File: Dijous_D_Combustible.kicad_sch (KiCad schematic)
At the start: 33 parts, among them J1 Conn_01x02, J2 DE9_Plug, J3 Conn_01x01, J4 Conn_02x03_Counter_Clockwise, U1 LM2596S-ADJ, U2 LM1117DT-ADJ, U3 MCP2551-I-SN, U4 PIC18F258-I/SO, U5 MCP4725xxx-xCH, Y2 Crystal

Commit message: Add files via upload
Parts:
- C4: value 680uF -> 120uF
- C5: value 3.3nF -> 1nF
- C6: value 220uF -> 470uF
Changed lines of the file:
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@@
 			)
 		)
-		(property "Value" "3.3nF"
+		(property "Value" "1nF"
 			(at 121.92 20.066 90)
 			(effects
@@
 			)
 		)
-		(property "Value" "220uF"
+		(property "Value" "470uF"
 			(at 148.59 55.8799 0)
 			(effects
@@
 			)
 		)
-		(property "Value" "680uF"
+		(property "Value" "120uF"
 			(at 87.63 50.7999 0)
 			(effects

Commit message: Add files via upload
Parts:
- removed J1: Conn_01x02, symbol Connector_Generic:Conn_01x02
- added J5: Screw_Terminal_01x02, symbol Connector:Screw_Terminal_01x02
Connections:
- net GNDPWR: now also J5.1 (Pin_1)
- net Vbat: now also J5.2 (Pin_2)
- net CanH: no longer names the net of C1.1, J2.7, R1.1, U3.7 (CANH)
- net CanL: no longer names the net of C1.2, J2.2, R1.2, U3.6 (CANL)
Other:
- note added: "Conector bateria"
- note added: "Conector botó apertura de combustible o tancament"
- note added: "Cristall"
- note added: "ISCP"
- note added: "Outputs"
- note removed: "Rellotge"
- moved on the sheet: C1, C10, C11, C2, C3, J2, J3, J4, R1, R10, R2, R3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

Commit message: Cambio de nombres
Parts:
- removed J3: Conn_01x01, symbol Connector_Generic:Conn_01x01
- added C12, C13: 100nF, symbol Device:C
- added D2, D3, D4, D5, D8: LED, LED_SMD:LED_0805_2012Metric, symbol Device:LED
- added D6, D7: D, symbol Device:D
- added J1: Conn_01x02, symbol Connector_Generic:Conn_01x02
- added K1, K2: Fujitsu_FTR-LYAA005x, Relay_THT:Relay_SPST-NO_Fujitsu_FTR-LYAA005x_FormA_Vertical, symbol Relay:Fujitsu_FTR-LYAA005x
- added Q1, Q2: 2SC4213, Package_TO_SOT_SMD:SOT-323_SC-70, symbol Transistor_BJT:2SC4213
- added R11, R12: 460, symbol Device:R
- added R13, R15: 510, symbol Device:R
- added R14, R16: 1k, symbol Device:R
- added R17: 515, symbol Device:R
- added R18: 0, symbol Device:R
- added R19, R20: 10K, symbol Device:R
- C3: value 10nF -> 100nF
- R10, R9: value 10K -> R
- Y2: value Crystal -> HC-49-US
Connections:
- net Boto: now also J1.2 (Pin_2)
- net GND: now also C3.2, R10.2, R9.2, C12.2, C13.1, R17.2, R18.2; no longer U1.3 (GND), U1.5 (~{ON}/OFF)
- net GNDPWR: now also U1.3 (GND), U1.5 (~{ON}/OFF), D2.1 (K), D3.1 (K), J1.1 (Pin_1), K1.13, K2.13, Q1.2 (E), Q2.2 (E), R18.1
- net LED_pneumatics: now also D8.2 (A)
- net SCA: now also R19.2; no longer R9.2
- net SCL: now also R20.2; no longer R10.2
- net VCC: now also C3.1, C12.1, C13.2, R19.1, R20.1; no longer R10.1, R9.1
- net Vbat: now also D6.1 (K), D7.1 (K), K1.A1, K2.A1, R11.1, R12.1, R13.1, R15.1
- new net: Q2.1 (B), R16.2
- new net: D4.1 (K), D6.2 (A), K1.A2, Q1.3 (C)
- new net: D5.1 (K), D7.2 (A), K2.A2, Q2.3 (C)
- new net: Q1.1 (B), R14.2
- new net: D8.1 (K), R17.1
- new net: D4.2 (A), R13.2
- new net: D3.2 (A), R12.2
- new net: D2.2 (A), R11.2
- new net: D5.2 (A), R15.2
- new net Bomba de combustible: K2.14
- new net R_Bomba: R10.1, R16.1
- new net R_Dipòsit: R14.1, R9.1
- new net Solenoide: K1.14
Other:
- note added: "LED POWER"
- note added: "LED POWER = Vermell"
- note added: "Outputs i Reles"
- note added: "RELAY STATUS LED"
- note added: "RELAY STATUS LED = Blau"
- note added: "Relè Bomba de Combustible"
- note added: "Relè Tancament Diposit"
- note added: "Sortida Pressió Pneumàtics"
- note added: "Unificació de GNDs"
- note added: "Vcc = 5V"
- note removed: "Outputs"
- moved on the sheet: C3

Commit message: Ultim canvi esquemàtic
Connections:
- net LED_pneumatics: now also U4.3 (RA1/AN1)
- net R_Bomba: now also U4.13 (RC2/CCP1)
- no-connect marks 11 -> 16
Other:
- moved on the sheet: D8, R17, R18, R19, R20

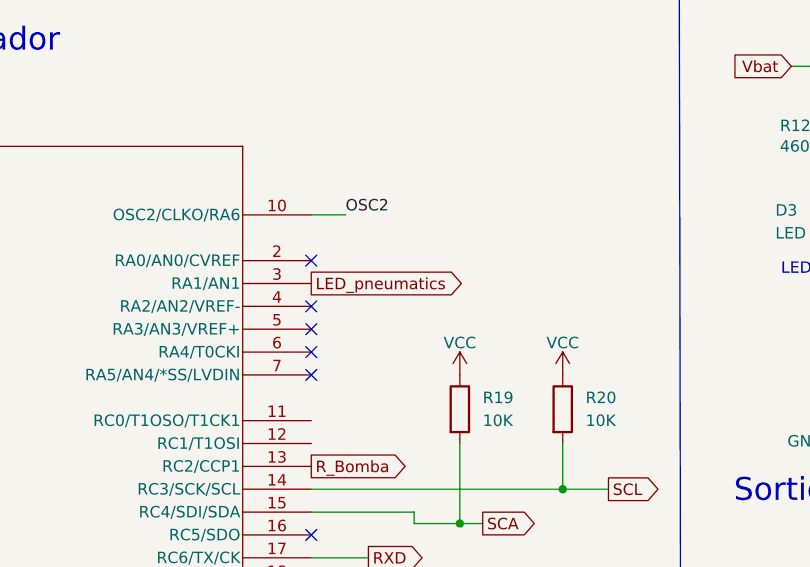
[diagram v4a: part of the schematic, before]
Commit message: Diagrama de blocs actualitzat i esquema
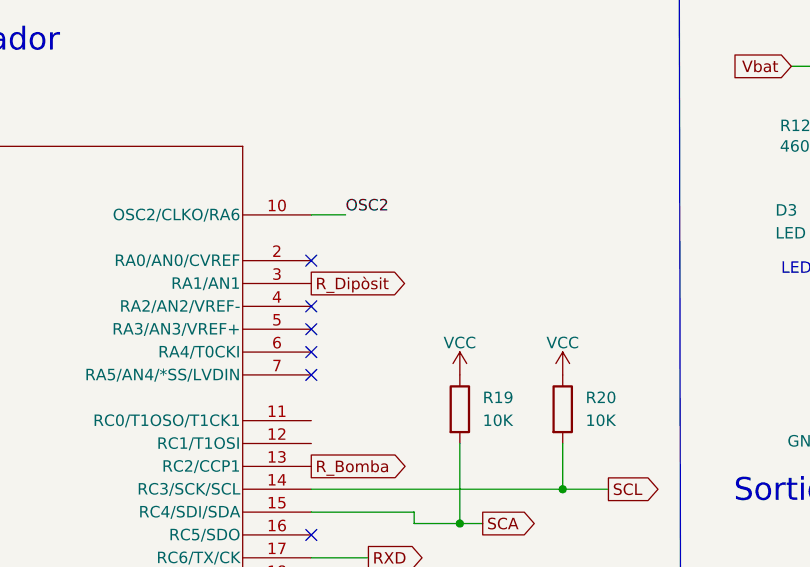
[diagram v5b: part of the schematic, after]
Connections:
- net LED_pneumatics: no longer U4.3 (RA1/AN1)
- net R_Dipòsit: now also U4.3 (RA1/AN1)
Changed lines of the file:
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@@
-		)
-	)
-	(global_label "LED_pneumatics"
-		(shape output)
-		(at 262.89 111.76 0)
-		(fields_autoplaced yes)
-		(effects
-			(font
-				(size 1.27 1.27)
-			)
-			(justify left)
-		)
-		(property "Intersheetrefs" "${INTERSHEET_REFS}"
-			(at 281.115 111.76 0)
-			(effects
-				(font
-					(size 1.27 1.27)
-				)
-				(justify left)
-				(hide yes)
-			)
 		)
 	)
@@
 				(hide yes)
 			)
+		)
+	)
+	(global_label "R_Dipòsit"
+		(shape output)
+		(at 262.89 111.76 0)
+		(fields_autoplaced yes)
+		(effects
+			(font
+				(size 1.27 1.27)
+			)
+			(justify left)
+		)
+		(property "Intersheetrefs" "${INTERSHEET_REFS}"
+			(at 274.6442 111.76 0)
+			(effects
+				(font
+					(size 1.27 1.27)
+				)
+				(justify left)
+				(hide yes)
+			)

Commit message: Readme & Esquemàtic
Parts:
- removed C2: 10nF, symbol Device:C
- removed C8: 11u, symbol Device:C
- removed D3: LED, LED_SMD:LED_0805_2012Metric, symbol Device:LED
- removed D6, D7: D, symbol Device:D
- removed J5: Screw_Terminal_01x02, symbol Connector:Screw_Terminal_01x02
- removed R7: 220, symbol Device:R
- removed R8: 680, symbol Device:R
- removed U2: LM1117DT-ADJ, Package_TO_SOT_SMD:TO-252-3_TabPin2, symbol Regulator_Linear:LM1117DT-ADJ
- added D10: MBR340, Diode_THT:D_DO-201AD_P15.24mm_Horizontal, symbol Diode:MBR340
- added D3, D6, D7, D9: 1N5408, Diode_THT:D_DO-201AD_P15.24mm_Horizontal, symbol Diode:1N5408
- added J3: Screw_Terminal_01x02, TerminalBlock:TerminalBlock_Altech_AK300-2_P5.00mm, symbol Connector:Screw_Terminal_01x02
- added U6: LM1117DT-5.0, Package_TO_SOT_SMD:TO-252-3_TabPin2, symbol Regulator_Linear:LM1117DT-5.0
- C1, C12, C13, C3: footprint (none) -> Capacitor_SMD:C_1206_3216Metric
- C5: footprint (none) -> Capacitor_SMD:C_0603_1608Metric
- C7: footprint (none) -> Capacitor_Tantalum_SMD:CP_EIA-3528-12_Kemet-T
- C9: footprint (none) -> Capacitor_Tantalum_SMD:CP_EIA-3216-12_Kemet-S
- J1: footprint (none) -> Connector_PinHeader_2.00mm:PinHeader_2x01_P2.00mm_Vertical
- J2: footprint (none) -> Connector_Dsub:DSUB-9_Male_Vertical_P2.77x2.84mm
- J4: footprint (none) -> Connector_PinHeader_2.54mm:PinHeader_2x03_P2.54mm_Vertical
- L1: footprint (none) -> Inductor_SMD:L_1206_3216Metric
- R1, R11, R13, R14, R15, R16, R17, R18, R19, R20, R4, R5, R6: footprint (none) -> Resistor_SMD:R_1206_3216Metric
- R10: value R -> 4,7k; footprint (none) -> Resistor_SMD:R_1206_3216Metric
- R12: value 460 -> 60; footprint (none) -> Resistor_SMD:R_1206_3216Metric
- R2, R3: value 10k -> 4,7k; footprint (none) -> Resistor_SMD:R_1206_3216Metric
- R9: value R -> 4.9K; footprint (none) -> Resistor_SMD:R_1206_3216Metric
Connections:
- net Bomba de combustible: now also D3.1 (K), D3.2 (A)
- net Boto: now also R2.1
- net GND: now also C1.2, J1.1 (Pin_1), R3.2, U6.1 (GND); no longer J2.3
- net GNDPWR: now also J3.1 (Pin_1); no longer J1.1 (Pin_1)
- net MCLR: now also R3.1
- net R_Bomba: no longer U4.13 (RC2/CCP1)
- net R_Dipòsit: no longer U4.3 (RA1/AN1)
- net Solenoide: now also D9.1 (K), D9.2 (A)
- net VCC: no longer C12.1, C13.2, C3.1, J4.2 (Pin_2), R3.1, U3.3 (VDD), U4.20 (VDD), U5.3 (VDD)
- net Vbat: now also D10.2 (A), D6.1 (K), D7.1 (K), J3.2 (Pin_2); no longer C4.1, R12.1, R5.2, U1.1 (VIN)
- net at D4.1 (K), K1.A2, Q1.3 (C): now also D6.2 (A)
- net at D5.1 (K), K2.A2, Q2.3 (C): now also D7.2 (A)
- net at J2.7, U3.7 (CANH): now also R12.1; no longer C1.1, R1.1
- net at J2.2, R1.2, U3.6 (CANL): no longer C1.2
- net at R12.2: now also C1.1, R1.1
- net at C5.2, C6.1, C7.1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: now also U6.3 (VI)
- net Vcc: no longer names the net of J2.9
- net Vcc: no longer C9.1
- new net: C4.1, D10.1 (K), R5.2, U1.1 (VIN)
- new net +5V: C12.1, C13.2, C3.1, C9.1, J4.2 (Pin_2), U3.3 (VDD), U4.20 (VDD), U5.3 (VDD), U6.2 (VO)
- now unconnected: U3.5 (Vref)
- no-connect marks 16 -> 23
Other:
- note added: "Freqüència del cristall = 8mhz"
- note removed: "Condensador datasheet"
- note removed: "Condensador:"
- moved on the sheet: C1, D5, D8, K2, Q2, R10, R15, R16, R17, R19, R20

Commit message: README & Layout
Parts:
- removed C12, C13: 100nF, Capacitor_SMD:C_1206_3216Metric, symbol Device:C
- removed D1: 1N5822, Diode_THT:D_DO-201AD_P15.24mm_Horizontal, symbol Diode:1N5822
- removed D10: MBR340, Diode_THT:D_DO-201AD_P15.24mm_Horizontal, symbol Diode:MBR340
- removed D2, D4, D5, D8: LED, LED_SMD:LED_0805_2012Metric, symbol Device:LED
- removed D3, D6, D7: 1N5408, Diode_THT:D_DO-201AD_P15.24mm_Horizontal, symbol Diode:1N5408
- removed J1: Conn_01x02, Connector_PinHeader_2.00mm:PinHeader_2x01_P2.00mm_Vertical, symbol Connector_Generic:Conn_01x02
- removed J2: DE9_Plug, Connector_Dsub:DSUB-9_Male_Vertical_P2.77x2.84mm, symbol Connector:DE9_Plug
- removed J3: Screw_Terminal_01x02, TerminalBlock:TerminalBlock_Altech_AK300-2_P5.00mm, symbol Connector:Screw_Terminal_01x02
- removed J4: Conn_02x03_Counter_Clockwise, Connector_PinHeader_2.54mm:PinHeader_2x03_P2.54mm_Vertical, symbol Connector_Generic:Conn_02x03_Counter_Clockwise
- removed R20: 10K, Resistor_SMD:R_1206_3216Metric, symbol Device:R
- removed U1: LM2596S-ADJ, Package_TO_SOT_SMD:TO-263-5_TabPin3, symbol Regulator_Switching:LM2596S-ADJ
- removed U3: MCP2551-I-SN, Package_SO:SOIC-8_3.9x4.9mm_P1.27mm, symbol Interface_CAN_LIN:MCP2551-I-SN
- removed U4: PIC18F258-I/SO, Librery_SOIC28:SOIC28-W_MC_MCH, symbol PIC18F258-I/SO:PIC18F258-I_SO
- removed U6: LM1117DT-5.0, Package_TO_SOT_SMD:TO-252-3_TabPin2, symbol Regulator_Linear:LM1117DT-5.0
- removed Y2: HC-49-US, Crystal:Crystal_SMD_HC49-SD, symbol Device:Crystal
- added C2: 120uF, Capacitor_SMD:CP_Elec_10x10, symbol Device:C
- added C8: 10u, Capacitor_Tantalum_SMD:CP_EIA-3528-12_Kemet-T, symbol Device:C
- added D1: MBR340, Diode_THT:D_DO-201AD_P15.24mm_Horizontal, symbol Diode:MBR340
- added D10, D3, D6, D7: LED, LED_SMD:LED_0805_2012Metric, symbol Device:LED
- added D2: 1N5822, Diode_THT:D_DO-201AD_P15.24mm_Horizontal, symbol Diode:1N5822
- added D4, D5, D8: 1N5408, Diode_THT:D_DO-201AD_P15.24mm_Horizontal, symbol Diode:1N5408
- added J1: Screw_Terminal_01x02, TerminalBlock:TerminalBlock_Altech_AK300-2_P5.00mm, symbol Connector:Screw_Terminal_01x02
- added J2: Conn_01x02, Connector_PinHeader_2.00mm:PinHeader_2x01_P2.00mm_Vertical, symbol Connector_Generic:Conn_01x02
- added J3: Conn_02x03_Counter_Clockwise, Connector_PinHeader_2.54mm:PinHeader_2x03_P2.54mm_Vertical, symbol Connector_Generic:Conn_02x03_Counter_Clockwise
- added J4: DE9_Plug, Connector_Dsub:DSUB-9_Male_Vertical_P2.77x2.84mm, symbol Connector:DE9_Plug
- added J5, J6, J7: Conn_01x02, Connector_PinHeader_2.54mm:PinHeader_1x02_P2.54mm_Vertical, symbol Connector_Generic:Conn_01x02
- added JP1: Jumper_3_Open, Connector:FanPinHeader_1x03_P2.54mm_Vertical, symbol Jumper:Jumper_3_Open
- added R7, R8: 4,7k, Resistor_SMD:R_1206_3216Metric, symbol Device:R
- added SW1: SW_Push, Button_Switch_SMD:SW_Push_SPST_NO_Alps_SKRK, symbol Switch:SW_Push
- added U1: MCP2551-I-SN, Package_SO:SOIC-8_3.9x4.9mm_P1.27mm, symbol Interface_CAN_LIN:MCP2551-I-SN
- added U2: LM2596S-ADJ, Package_TO_SOT_SMD:TO-263-5_TabPin3, symbol Regulator_Switching:LM2596S-ADJ
- added U3: PIC18F258-I/SO, Librery_SOIC28:SOIC28-W_MC_MCH, symbol PIC18F258-I/SO:PIC18F258-I_SO
- added U4: LM1117DT-5.0, Package_TO_SOT_SMD:TO-252-3_TabPin2, symbol Regulator_Linear:LM1117DT-5.0
- added Y1: HC-49-US, Crystal:Crystal_SMD_HC49-SD, symbol Device:Crystal
- C1: value 100pF -> 100nF
- C10: value 15p -> 22u; footprint Capacitor_SMD:C_0805_2012Metric -> Capacitor_Tantalum_SMD:CP_EIA-3216-12_Kemet-S
- C11: value 15p -> 100nF; footprint Capacitor_SMD:C_0805_2012Metric -> Capacitor_SMD:C_1206_3216Metric
- C3: value 100nF -> 15p; footprint Capacitor_SMD:C_1206_3216Metric -> Capacitor_SMD:C_0805_2012Metric
- C4: value 120uF -> 100pF; footprint Capacitor_THT:CP_Radial_D10.0mm_P5.00mm -> Capacitor_SMD:C_1206_3216Metric
- C5: value 1nF -> 15p; footprint Capacitor_SMD:C_0603_1608Metric -> Capacitor_SMD:C_0805_2012Metric
- C6: value 470uF -> 1nF; footprint Capacitor_SMD:CP_Elec_10x10 -> Capacitor_SMD:C_0603_1608Metric
- C7: value 10u -> 470uF; footprint Capacitor_Tantalum_SMD:CP_EIA-3528-12_Kemet-T -> Capacitor_SMD:CP_Elec_10x10
- C9: value 22u -> 100nF; footprint Capacitor_Tantalum_SMD:CP_EIA-3216-12_Kemet-S -> Capacitor_SMD:C_1206_3216Metric
- R1: value 60 -> 15k
- R10: value 4,7k -> 510
- R11: value 460 -> 4,7k
- R12: value 60 -> 1k
- R13: value 510 -> 10K
- R14: value 1k -> 10K
- R15: value 510 -> 460
- R16: value 1k -> 510
- R17: value 515 -> 4.7K
- R18: value 0 -> 1k
- R19: value 10K -> 515
- R2, R3: value 4,7k -> 60
- R4: value 15k -> 0
- R9: value 4.9K -> 10k; footprint Resistor_SMD:R_1206_3216Metric -> Resistor_SMD:R_0805_2012Metric
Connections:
- net Bomba de combustible is gone; now on net Vbat: K2.14
- net +5V: now also C1.1, C10.1, C11.1, C9.2, R13.1, R14.1, R9.1, J3.2 (Pin_2), U1.3 (VDD), U3.20 (VDD), U4.2 (VO); no longer C3.1, C9.1
- net Boto: now also J2.2 (Pin_2), R8.1, U3.21 (RB0/INT0); no longer R2.1
- net GND: now also C11.2, C5.1, C9.1, R1.2, R11.2, R19.2, C8.2, J2.1 (Pin_1), J3.3 (Pin_3), J6.2 (Pin_2), R7.2, R8.2, SW1.2, U1.2 (VSS), U3.19 (VSS), U3.8 (VSS), U4.1 (GND); no longer C11.1, C6.2, C7.2, C9.2, R10.2, R18.2, R2.2, R3.2, R9.2
- net GNDPWR: now also C7.2, D9.2 (A), R4.1, C2.2, D2.2 (A), D5.2 (A), D6.1 (K), J1.1 (Pin_1), J5.2 (Pin_2), J7.2 (Pin_2), U2.3 (GND), U2.5 (~{ON}/OFF); no longer K1.13, K2.13, R18.1
- net LED_pneumatics: now also D10.2 (A), U3.22 (RB1/INT1)
- net MCLR: now also J3.1 (Pin_1), JP1.1 (A), R7.1; no longer R3.1
- net Nivell_combustible: now also J6.1 (Pin_1)
- net OSC1: now also C3.1, U3.9 (OSC1/CLKI), Y1.1; no longer C10.1
- net OSC2: now also C5.2, U3.10 (OSC2/CLKO/RA6), Y1.2; no longer C11.2
- net PGC: now also J3.5 (Pin_5), U3.27 (RB6/PGC)
- net PGD: now also J3.4 (Pin_4), U3.28 (RB7/PGD)
- net RXD: now also U1.4 (RXD), U3.17 (RC6/TX/CK)
- net R_Bomba: now also R11.1, R12.1, U3.13 (RC2/CCP1); no longer R10.1, R16.1
- net R_Dipòsit: now also R17.1, R18.1, U3.3 (RA1/AN1); no longer R14.1, R9.1
- net SCA: now also R13.2, U3.15 (RC4/SDI/SDA); no longer R19.2
- net SCL: now also R14.2, U3.14 (RC3/SCK/SCL)
- net Solenoide: now also K2.13, J5.1 (Pin_1); no longer D9.2 (A), K1.14
- net TXD: now also U1.1 (TXD), U3.18 (RC7/RX/DT)
- net Vbat: now also K1.14, R10.1, R16.1, D1.2 (A), D4.1 (K), D8.1 (K), J1.2 (Pin_2); no longer R11.1, R13.1
- net at Q2.1 (B): now also R18.2; no longer R16.2
- net Retorn_sol: now reaches K1.A2, Q1.3 (C)
- net Retorn_sol: now also D3.1 (K), D4.2 (A)
- net at Q1.1 (B): now also R12.2; no longer R14.2
- net Vin_LDO: now reaches C7.1, L1.1, R6.2
- net Vin_LDO: now also C6.2, C8.1, U4.3 (VI); no longer C5.2, C6.1
- net at C4.1: now also R2.2, R3.1; no longer R5.2
- net Vout_Buck: now reaches L1.2
- net Vout_Buck: now also D2.1 (K), U2.2 (OUT)
- net at R5.1, R6.1: now also C6.1, U2.4 (FB); no longer C5.1
- net Retorn_dip: now reaches K2.A2, Q2.3 (C)
- net Retorn_dip: now also D7.1 (K), D8.2 (A)
- net at R15.2: now also D6.2 (A)
- net VCC: no longer names the net of R19.1
- net VCC: now also D10.1 (K)
- new net: R1.1, U1.8 (Rs)
- new net: D3.2 (A), R10.2
- new net: D7.2 (A), R16.2
- new net: JP1.3 (B), R9.2, SW1.1
- new net: JP1.2 (C), U3.1 (*MCLR/VPP)
- new net Bomba_combustible: D5.1 (K), J7.1 (Pin_1), K1.13
- new net Can+: J4.7, R2.1, U1.7 (CANH)
- new net Can-: J4.2, R3.2, U1.6 (CANL)
- new net Vin_Buck: C2.1, D1.1 (K), R5.2, U2.1 (VIN)
- no-connect marks 23 -> 21
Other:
- note added: "Autors: Raúl Carod Martinez Sergi Pacheco i Ortiz"
- note added: "Bomba de combustible"
- note added: "DAC"
- note added: "Freqüència del cristall = 4Mhz"
- note added: "Outputs"
- note added: "RESET MICROCONTROLADOR"
- note added: "Relès"
- note added: "Sortida tancament de dipòsit"
- note removed: "Freqüència del cristall = 8mhz"
- note removed: "Outputs i Reles"
